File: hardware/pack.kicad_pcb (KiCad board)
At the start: 2 copper layers, 140 x 100 mm, 124 parts, among them U1 MT3608

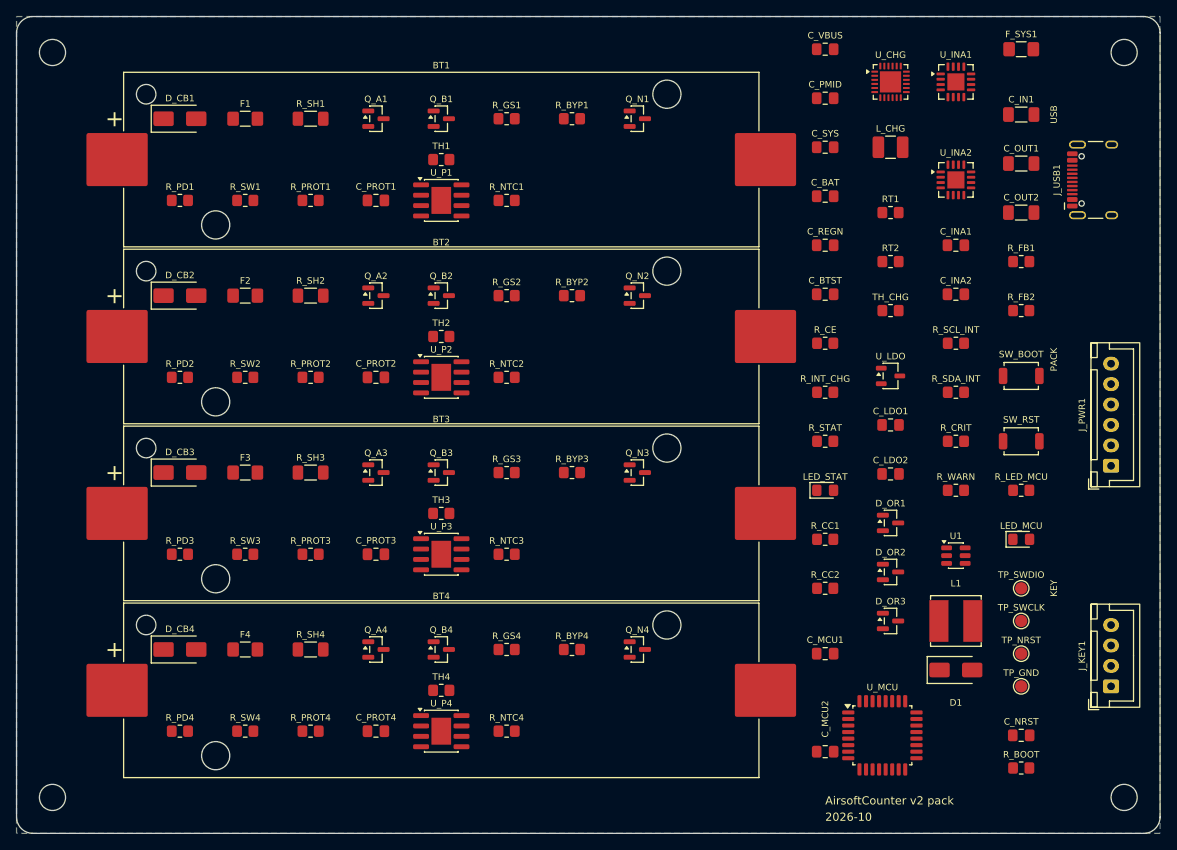
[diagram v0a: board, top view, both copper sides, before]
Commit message: hardware: pack board routing and fab package (P4.2)
The QFN24/VQFN16 pads cannot take a 0.8 mm Power trunk, so the shunt
Kelvin sense now splits through an 0R into the INA3221 (plan P4.2), and the
two INA3221s sit in a cell's free middle band next to their shunts.
Freerouting: 7 passes, 0 unrouted; DRC --schematic-parity: 0 violations.
make BOARD=pack fab writes fab/pack/; make boards is green for both boards.

check_gerbers.py: NPTH_EXPECT / PTH_COMPONENT_MIN come from the board
module (the pack's holders and USB-C legitimately add drills).
gen_sch/gen_pcb: NOT_ASSEMBLED parts agree on in_bom; HIDE_REF.

Co-Authored-By: Claude Opus 5.5 <noreply@anthropic.com>
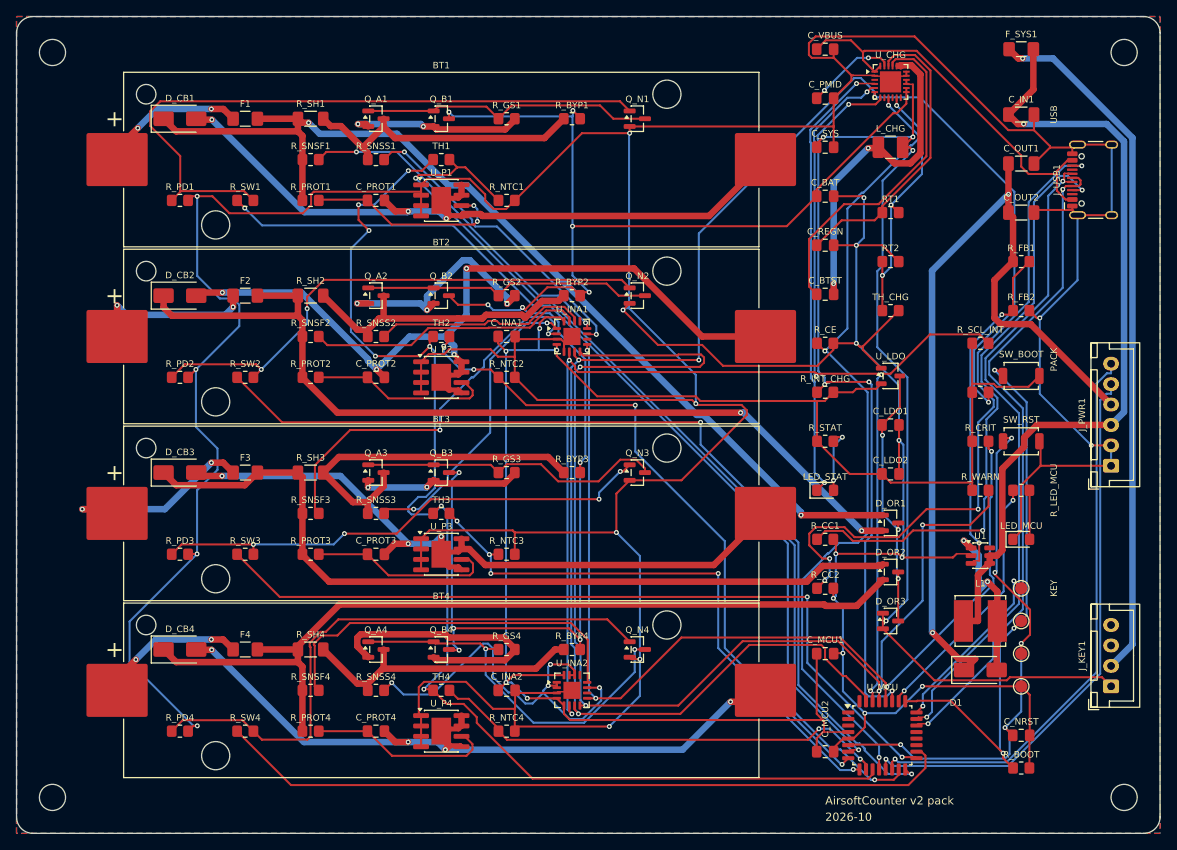
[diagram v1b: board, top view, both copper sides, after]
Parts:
- added R_SNSF1: 0R, Resistor_SMD:R_0805_2012Metric_Pad1.20x1.40mm_HandSolder, F.Cu at (36.0, 17.5)
- added R_SNSF2: 0R, Resistor_SMD:R_0805_2012Metric_Pad1.20x1.40mm_HandSolder, F.Cu at (36.0, 39.2)
- added R_SNSF3: 0R, Resistor_SMD:R_0805_2012Metric_Pad1.20x1.40mm_HandSolder, F.Cu at (36.0, 60.8)
- added R_SNSF4: 0R, Resistor_SMD:R_0805_2012Metric_Pad1.20x1.40mm_HandSolder, F.Cu at (36.0, 82.5)
- added R_SNSS1: 0R, Resistor_SMD:R_0805_2012Metric_Pad1.20x1.40mm_HandSolder, F.Cu at (44.0, 17.5)
- added R_SNSS2: 0R, Resistor_SMD:R_0805_2012Metric_Pad1.20x1.40mm_HandSolder, F.Cu at (44.0, 39.2)
- added R_SNSS3: 0R, Resistor_SMD:R_0805_2012Metric_Pad1.20x1.40mm_HandSolder, F.Cu at (44.0, 60.8)
- added R_SNSS4: 0R, Resistor_SMD:R_0805_2012Metric_Pad1.20x1.40mm_HandSolder, F.Cu at (44.0, 82.5)
- moved U_INA2 78.2 mm to (68.0, 82.5)
- moved C_INA2 73.3 mm to (60.0, 82.5)
- moved U_INA1 56.4 mm to (68.0, 39.2)
- moved C_INA1 56.1 mm to (60.0, 39.2)
- moved D1 3.00 mm to (118.0, 80.0)
- moved L1 3.00 mm to (118.0, 74.0)
- moved R_CRIT 3.00 mm to (118.0, 52.0)
- moved R_SCL_INT 3.00 mm to (118.0, 40.0)
- moved R_SDA_INT 3.00 mm to (118.0, 46.0)
- moved R_WARN 3.00 mm to (118.0, 58.0)
- moved U1 3.00 mm to (118.0, 66.0)
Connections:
- U_INA1 pad 1: CELL3_S -> INA_S3
- U_INA1 pad 11: CELL1_S -> INA_S1
- U_INA1 pad 12: CELL1_F -> INA_F1
- U_INA1 pad 14: CELL2_S -> INA_S2
- U_INA1 pad 15: CELL2_F -> INA_F2
- U_INA1 pad 2: CELL3_F -> INA_F3
- U_INA2 pad 1: CELL4_S -> INA_S4
- U_INA2 pad 11: CELL4_S -> INA_S4
- U_INA2 pad 12: CELL4_F -> INA_F4
- U_INA2 pad 14: CELL4_S -> INA_S4
- U_INA2 pad 15: CELL4_S -> INA_S4
- U_INA2 pad 2: CELL4_S -> INA_S4
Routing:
- net GND: track 0.00 -> 748.4 mm, vias 0 -> 22
- net +3V3: track 0.00 -> 219.0 mm, vias 0 -> 5
- net SDA_INT: track 0.00 -> 202.4 mm, vias 0 -> 5
- net VPACK: track 0.00 -> 199.2 mm, vias 0 -> 11
- net SCL_INT: track 0.00 -> 181.3 mm, vias 0 -> 6
- net NTC_PWR: track 0.00 -> 154.1 mm, vias 0 -> 7
- net INA_WARN: track 0.00 -> 151.7 mm, vias 0 -> 4
- net INA_CRIT: track 0.00 -> 124.2 mm, vias 0 -> 4
- net CELL1_F: track 0.00 -> 124.2 mm, vias 0 -> 2
- net SW1_DRV: track 0.00 -> 122.9 mm, vias 0 -> 2
- net SYS: track 0.00 -> 119.0 mm, vias 0 -> 4
- net SW2_DRV: track 0.00 -> 115.7 mm, vias 0 -> 2
- net CELL2_F: track 0.00 -> 112.4 mm, vias 0 -> 2
- net NTC1: track 0.00 -> 108.4 mm, vias 0 -> 2
- net CELL4_F: track 0.00 -> 107.8 mm
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- added copper zone on F.Cu, net GND

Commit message: hardware: pack board 96x90 with bottom-side MYOUNG holders
The Keystone 1042 holders were only 14.86 mm tall around an 18.3 mm
cell, so parts placed under them could not fit. Swap to MYOUNG
BH-18650-A6AJ012 (C19184084, THT, footprint in local.pretty from drawing
MY-CP-0373) on the bottom side, with the MF52 bead NTCs in the holder
floor window; every SMD part stays on top for single-side assembly. The
board shrinks from 140 x 100 to 96 x 90 mm.

gen_pcb.py: BOTTOM set flips footprints, project fp-lib-table adds the
local library. VPACK/SYS split from the BQ25601 pins through 1206 0R
jumpers so the rails can take the 0.8 mm Power class.

make boards is green (ERC, DRC parity, gerbers, jlc).

Co-Authored-By: Claude Opus 5.5 <noreply@anthropic.com>
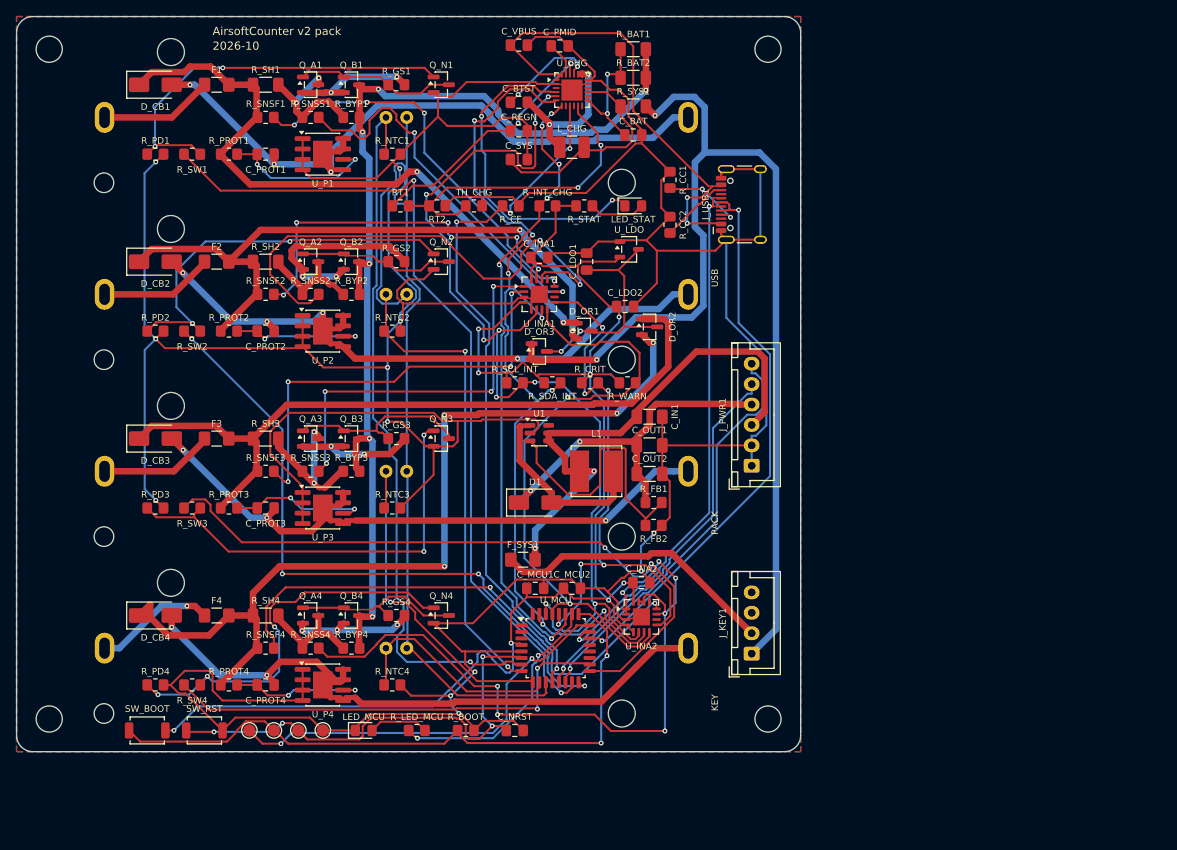
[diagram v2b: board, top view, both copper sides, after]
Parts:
- added R_BAT1: 0R, Resistor_SMD:R_1206_3216Metric_Pad1.30x1.75mm_HandSolder, F.Cu at (75.5, 4.00)
- added R_BAT2: 0R, Resistor_SMD:R_1206_3216Metric_Pad1.30x1.75mm_HandSolder, F.Cu at (75.5, 7.50)
- added R_SYS1: 0R, Resistor_SMD:R_1206_3216Metric_Pad1.30x1.75mm_HandSolder, F.Cu at (75.5, 11.0)
- BT1, BT2, BT3, BT4: footprint Battery:BatteryHolder_Keystone_1042_1x18650 -> local:BatteryHolder_MYOUNG_BH-18650-A6AJ012; moved to B.Cu
- TH1, TH2, TH3, TH4: footprint Resistor_SMD:R_0805_2012Metric_Pad1.20x1.40mm_HandSolder -> local:NTC_Bead_P2.54mm; moved to B.Cu
- moved SW_BOOT 115.5 mm to (16.0, 87.4)
- moved SW_RST 106.1 mm to (23.0, 87.4)
- moved TP_SWDIO 96.1 mm to (28.5, 87.4)
- moved TP_SWCLK 92.5 mm to (31.5, 87.4)
- moved TP_NRST 89.0 mm to (34.5, 87.4)
- moved F_SYS1 87.3 mm to (62.0, 66.5)
- moved TP_GND 85.7 mm to (37.5, 87.4)
- moved LED_MCU 83.8 mm to (42.5, 87.4)
- moved R_LED_MCU 79.6 mm to (49.0, 87.4)
- moved R_BOOT 68.2 mm to (55.0, 87.4)
- moved C_NRST 62.0 mm to (61.0, 87.4)
- moved RT1 60.0 mm to (47.0, 23.2)
- moved C_IN1 58.6 mm to (77.5, 49.0)
- moved D1 58.2 mm to (63.5, 59.5)
- moved R_SCL_INT 57.2 mm to (61.0, 44.8)
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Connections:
- C_BAT pad 1: VPACK -> BAT_CHG
- C_SYS pad 1: SYS -> SYS_CHG
- L_CHG pad 2: SYS -> SYS_CHG
- U_CHG pad 13: VPACK -> BAT_CHG
- U_CHG pad 14: VPACK -> BAT_CHG
- U_CHG pad 15: SYS -> SYS_CHG
- U_CHG pad 16: SYS -> SYS_CHG
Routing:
- net GND: track 748.4 -> 606.1 mm, vias 22 -> 12
- net SDA_INT: track 202.4 -> 113.2 mm, vias 5 -> 7
- net INA_WARN: track 151.7 -> 73.7 mm, vias 4 -> 2
- net CC2: track 83.1 -> 8.43 mm, vias 4 -> 0
- net VPACK: track 199.2 -> 127.5 mm, vias 11 -> 6
- net CC1: track 75.3 -> 10.2 mm
- net +5V: track 104.8 -> 42.7 mm
- net SCL_INT: track 181.3 -> 123.4 mm, vias 6 -> 9
- net INA_CRIT: track 124.2 -> 69.4 mm, vias 4 -> 6
- net KEY_OUT: track 85.3 -> 35.1 mm, vias 1 -> 0
- net CELL1_F: track 124.2 -> 80.2 mm
- net INA_S4: track 51.2 -> 88.7 mm, vias 4 -> 7
- net NTC_PWR: track 154.1 -> 116.8 mm, vias 7 -> 0
- net INA_S2: track 26.2 -> 62.9 mm, vias 0 -> 2
- net VBAT_SW: track 98.5 -> 63.0 mm, vias 1 -> 2
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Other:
- board size 140 x 100 mm -> 96 x 90 mm

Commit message: hardware: pack board without protector ICs, Basic diode-OR and TS pair
Cost cut after a ~$140 quote for 5 assembled boards (15 SMD Extended
types at ~$3 each). The per-cell MCU switches already default off, so a
dead or reset MCU leaves every cell open; with the 5 A fuses and the
BQ25601's CV/OVP they cover what the four XB8089D did. Holder- now goes
straight to GND. A single shared protector was rejected: with all
switches open the pack rail is 0 V and it would cut the MCU's ground
return, so the board could never boot.

- U_P1-4, R_PROT1-4, C_PROT1-4 removed.
- Diode-OR: 3x BAT54C -> 5x B5819W SOD-123 (C8598, Basic), one per
  cell in its own band and D_OR5 for SYS.
- TS bias 5.23k/30.9k -> 5.1k/30k (Basic): window 0/60 C -> 0.5/60.8 C.
- Sense taps 0R -> 10R: a reversed cell's crowbar now pulls the INA3221
  inputs below -0.3 V until the fuse clears; 10 Ohm limits the clamp
  current.
- power_budget.py drops the XB8089D current.

11 SMD Extended types (was 15), 105 placements (was 115).
make BOARD=pack all is green (ERC, DRC parity, gerbers, jlc).

Co-Authored-By: Claude Opus 5.5 <noreply@anthropic.com>
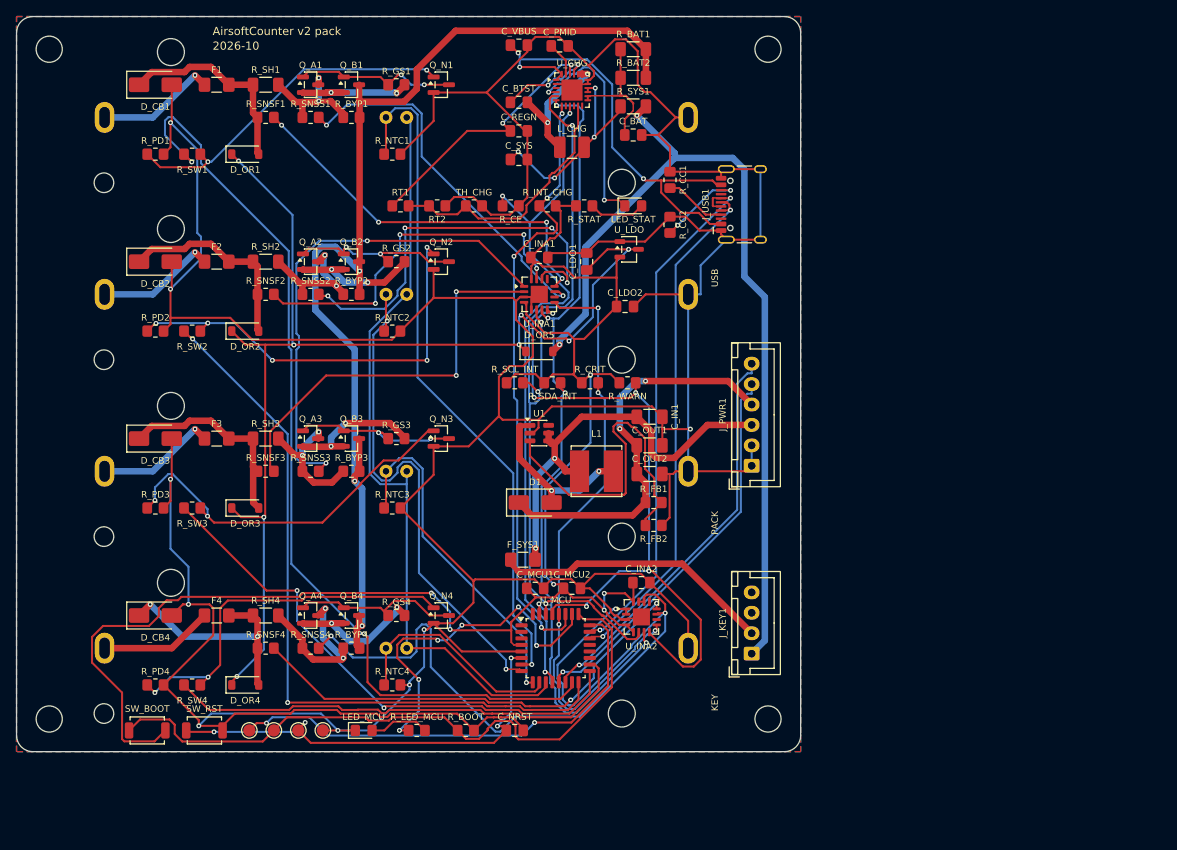
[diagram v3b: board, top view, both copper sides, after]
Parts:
- removed C_PROT1, C_PROT2, C_PROT3, C_PROT4: 100nF, Capacitor_SMD:C_0805_2012Metric_Pad1.18x1.45mm_HandSolder
- removed R_PROT1, R_PROT2, R_PROT3, R_PROT4: 1k, Resistor_SMD:R_0805_2012Metric_Pad1.20x1.40mm_HandSolder
- removed U_P1, U_P2, U_P3, U_P4: XB8089D, Package_SO:SOIC-8-1EP_3.9x4.9mm_P1.27mm_EP2.41x3.3mm
- added D_OR4: B5819W, Diode_SMD:D_SOD-123, F.Cu at (28.0, 81.8)
- added D_OR5: B5819W, Diode_SMD:D_SOD-123, F.Cu at (64.0, 41.0)
- D_OR1, D_OR2, D_OR3: value BAT54C -> B5819W; footprint Package_TO_SOT_SMD:SOT-23 -> Diode_SMD:D_SOD-123
- RT1: value 5k23 -> 5k1
- RT2: value 30k9 -> 30k
- R_SNSF1, R_SNSF2, R_SNSF3, R_SNSF4, R_SNSS1, R_SNSS2, R_SNSS3, R_SNSS4: value 0R -> 10R
- moved D_OR2 49.5 mm to (28.0, 38.5)
- moved D_OR1 46.8 mm to (28.0, 16.9)
- moved D_OR3 40.8 mm to (28.0, 60.2)
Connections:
- BT1 pad 2: CELL1_N -> GND
- BT2 pad 2: CELL2_N -> GND
- BT3 pad 2: CELL3_N -> GND
- BT4 pad 2: CELL4_N -> GND
- D_CB1 pad 2: CELL1_N -> GND
- D_CB2 pad 2: CELL2_N -> GND
- D_CB3 pad 2: CELL3_N -> GND
- D_CB4 pad 2: CELL4_N -> GND
- D_OR1 pad 1: CELL1_F -> VMCU_IN
- D_OR1 pad 2: CELL2_F -> CELL1_F
- D_OR2 pad 1: CELL3_F -> VMCU_IN
- D_OR2 pad 2: CELL4_F -> CELL2_F
- D_OR3 pad 1: SYS -> VMCU_IN
- D_OR3 pad 2: SYS -> CELL3_F
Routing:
- net VMCU_IN: track 29.7 -> 143.9 mm, vias 2 -> 8
- net CELL1_N: track 84.7 -> 0.00 mm, vias 3 -> 0
- net CELL4_N: track 81.2 -> 0.00 mm, vias 2 -> 0
- net CELL2_N: track 79.8 -> 0.00 mm, vias 4 -> 0
- net CELL4_F: track 108.2 -> 28.5 mm, vias 4 -> 2
- net CELL3_N: track 78.5 -> 0.00 mm, vias 3 -> 0
- net CELL3_F: track 89.1 -> 25.3 mm
- net CELL1_F: track 80.2 -> 24.5 mm, vias 2 -> 0
- net CELL2_F: track 79.3 -> 24.5 mm, vias 2 -> 0
- net SCL_INT: track 123.4 -> 99.5 mm, vias 9 -> 4
- net NTC_PWR: track 116.8 -> 93.0 mm
- net SYS: track 130.4 -> 108.6 mm
- net GND: track 606.1 -> 584.5 mm, vias 12 -> 9
- net PROT1_VDD: track 18.9 -> 0.00 mm, vias 2 -> 0
- net +3V3: track 189.6 -> 207.1 mm, vias 8 -> 6
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
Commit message: hardware: one PAC1934 replaces the two INA3221s on the pack board
Four channels in one chip (C623960, UQFN-16 4x4, KiCad
Sensor_Energy:PAC1934x-xJQ), cell n on channel n, with on-chip power
accumulators for coulomb counting. VBUS is read at SENSE+, which sits on
the fuse side of the shunt, so each channel still sees its own cell with
the switch open. ADDRSEL to GND = 0x10. SLOW/ALERT and PWRDN take the
two MCU pins the INA alerts used (28, 29), both pulled up so the monitor
runs without firmware; the pull-ups sit beside the MCU.

Shunt 20 -> 10 mOhm (FMF06FTHR010-LH, C105362, 1 W): the PAC1934 allows
only 500 mV across its sense pins, and with no protector IC a hard short
drives about 25 A per cell until the fuse clears. +-10 A full scale.

power_budget.py: monitor at its 5 uA SLEEP (PWRDN drops the
configuration), pack key-off 112 uA.

104 placements, 11 SMD Extended types; make BOARD=pack all is green.

Co-Authored-By: Claude Opus 5.5 <noreply@anthropic.com>
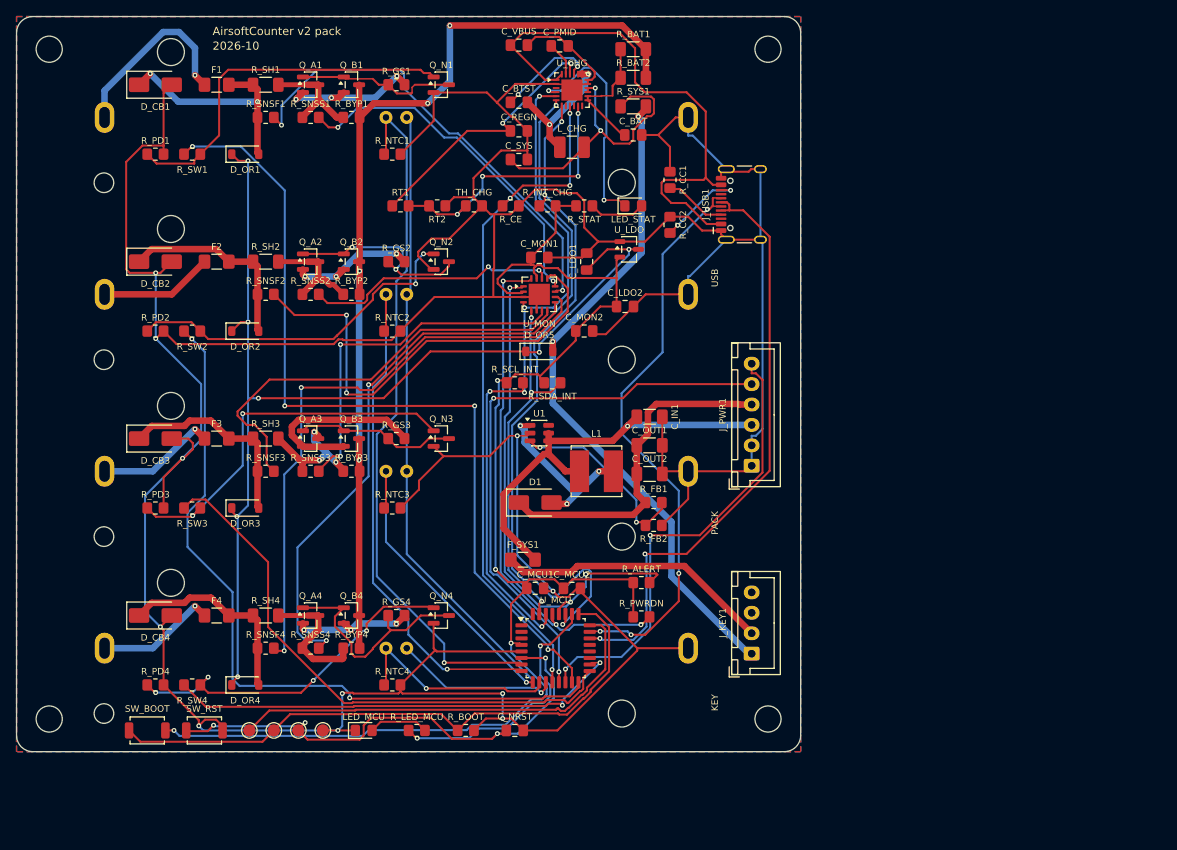
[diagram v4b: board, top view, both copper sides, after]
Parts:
- removed C_INA1, C_INA2: 100nF, Capacitor_SMD:C_0805_2012Metric_Pad1.18x1.45mm_HandSolder
- removed R_CRIT, R_WARN: 10k, Resistor_SMD:R_0805_2012Metric_Pad1.20x1.40mm_HandSolder
- removed U_INA1, U_INA2: INA3221, Package_DFN_QFN:Texas_RGV0016A_VQFN-16-1EP_4x4mm_P0.65mm_EP2.1x2.1mm
- added C_MON1: 100nF, Capacitor_SMD:C_0805_2012Metric_Pad1.18x1.45mm_HandSolder, F.Cu at (64.0, 29.5)
- added C_MON2: 100nF, Capacitor_SMD:C_0805_2012Metric_Pad1.18x1.45mm_HandSolder, F.Cu at (69.5, 38.5)
- added R_ALERT: 10k, Resistor_SMD:R_0805_2012Metric_Pad1.20x1.40mm_HandSolder, F.Cu at (76.5, 69.3)
- added R_PWRDN: 10k, Resistor_SMD:R_0805_2012Metric_Pad1.20x1.40mm_HandSolder, F.Cu at (76.5, 73.5)
- added U_MON: PAC1934T-I/JQ, Package_DFN_QFN:UQFN-16-1EP_4x4mm_P0.65mm_EP2.6x2.6mm, F.Cu at (64.0, 34.0)
- R_SH1, R_SH2, R_SH3, R_SH4: value 20mOhm -> 10mOhm
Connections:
- R_SNSF1 pad 2: INA_F1 -> SNS_F1
- R_SNSF2 pad 2: INA_F2 -> SNS_F2
- R_SNSF3 pad 2: INA_F3 -> SNS_F3
- R_SNSF4 pad 2: INA_F4 -> SNS_F4
- R_SNSS1 pad 2: INA_S1 -> SNS_S1
- R_SNSS2 pad 2: INA_S2 -> SNS_S2
- R_SNSS3 pad 2: INA_S3 -> SNS_S3
- R_SNSS4 pad 2: INA_S4 -> SNS_S4
- U_MCU pad 28: INA_CRIT -> MON_ALERT
- U_MCU pad 29: INA_WARN -> MON_PWRDN
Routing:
- net INA_S4: track 103.5 -> 0.00 mm, vias 3 -> 0
- net INA_WARN: track 86.4 -> 0.00 mm, vias 5 -> 0
- net INA_CRIT: track 76.5 -> 0.00 mm, vias 4 -> 0
- net SNS_F4: track 0.00 -> 72.8 mm, vias 0 -> 2
- net SNS_S4: track 0.00 -> 66.9 mm, vias 0 -> 2
- net MON_ALERT: track 0.00 -> 63.6 mm, vias 0 -> 3
- net MON_PWRDN: track 0.00 -> 62.7 mm, vias 0 -> 3
- net INA_S3: track 60.7 -> 0.00 mm, vias 2 -> 0
- net SNS_F2: track 0.00 -> 57.0 mm, vias 0 -> 2
- net SNS_F1: track 0.00 -> 56.9 mm, vias 0 -> 2
- net INA_F4: track 56.6 -> 0.00 mm, vias 2 -> 0
- net SNS_F3: track 0.00 -> 53.1 mm
- net INA_S2: track 50.0 -> 0.00 mm, vias 4 -> 0
- net INA_F3: track 49.2 -> 0.00 mm, vias 2 -> 0
- net INA_F1: track 47.7 -> 0.00 mm, vias 4 -> 0
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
